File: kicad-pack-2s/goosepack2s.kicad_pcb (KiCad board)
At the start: 4 copper layers, 67 parts, among them J1 USB_C_Receptacle_USB2.0_16P, J11 Balance 2S, J2 Pack lead, J3 XT30UPB-M, Q2 IRF8736, Q3 IRF8736, Q4 AO3400A, Q5 AO3400A, U13 S-8252AAH, U21 HY2213-BB3A, U22 HY2213-BB3A, U7 BQ25798

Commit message: Fill in LCSC numbers, swap to stocked parts, tidy the new schematic parts
- LCSC numbers from JLC's 2026-10-19 in-stock catalog for every new part
  except the DRV8251A, which JLC doesn't stock (Global Sourcing or consign).
- 2S protector S-8252AAH -> HY2120-LB (C168778): pin-for-pin the same,
  OV 4.25 V / UV 2.80 V, stocked at JLC. R94 trip recovery still holds.
- IPROPI R101-R106 1.18k (2,341 in stock) -> 1.2k preferred (C25862),
  so the motor limit is 1.34 A.
- Fix the 2S pack board's footprint-symbol links (paths were dropped in
  the previous commit); both boards now link every footprint correctly.
- Move the VREF divider and the balancer block into clear space and
  rewrite the stale DRV8871/BQ7791501 notes on the motor and 2S sheets.

Co-Authored-By: Claude Opus 5.5 <noreply@anthropic.com>
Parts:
- U13: value S-8252AAH -> HY2120-LB
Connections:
- net /PROT_VM renamed /PROT_CS
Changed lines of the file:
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@@
 				(font
 					(size 1.27 1.27)
+					(thickness 0.15)
 				)
 			)
@@
 				(font
 					(size 1.27 1.27)
+					(thickness 0.15)
 				)
 			)
 		)
-		(property "LCSC Part #" ""
+		(property "LCSC Part #" "C144394"
 			(at 0 0 0)
 			(layer "F.Fab")
@@
 				(font
 					(size 1.27 1.27)
+					(thickness 0.15)
 				)
 			)
@@
 			)
 		)
-		(property "LCSC Part #" ""
+		(property "LCSC Part #" "C25762"
 			(at 0 0 0)
 			(layer "F.Fab")
@@
 				(font
 					(size 1.27 1.27)
+					(thickness 0.15)
 				)
 			)
@@
 				(font
 					(size 1.27 1.27)
+					(thickness 0.15)
 				)
 			)
@@
 				(font
 					(size 1.27 1.27)
+					(thickness 0.15)
 				)
 			)
@@
 				(font
 					(size 1.27 1.27)
+					(thickness 0.15)
 				)
 			)
@@
 				(font
 					(size 1.27 1.27)
+					(thickness 0.15)
 				)
 			)
@@
 				(font
 					(size 1.27 1.27)
+					(thickness 0.15)
 				)
 			)
@@
 				(font
 					(size 1.27 1.27)
+					(thickness 0.15)
 				)
 			)
@@
 				(font
 					(size 1.27 1.27)
+					(thickness 0.15)
 				)
 			)
@@
 				(font
 					(size 1.27 1.27)
+					(thickness 0.15)
 				)
 			)
@@
 				(font
 					(size 1.27 1.27)
+					(thickness 0.15)
 				)
 			)
@@
 				(font
 					(size 1.27 1.27)
+					(thickness 0.15)
 				)
 			)
@@
 				(font
 					(size 1.27 1.27)
+					(thickness 0.15)
 				)
 			)
@@
 				(font
 					(size 1.27 1.27)
+					(thickness 0.15)
 				)
 			)
@@
 				(font
 					(size 1.27 1.27)
+					(thickness 0.15)
 				)
 			)
@@
 				(font
 					(size 1.27 1.27)
+					(thickness 0.15)
 				)
 			)
@@
 			)
 		)
-		(property "LCSC Part #" ""
+		(property "LCSC Part #" "C25117"
 			(at 0 0 0)
 			(layer "F.Fab")
@@
 				(font
 					(size 1.27 1.27)
+					(thickness 0.15)
 				)
 			)
@@
 				(font
 					(size 1.27 1.27)
+					(thickness 0.15)
 				)
 			)
@@
 				(font
 					(size 1.27 1.27)
+					(thickness 0.15)
 				)
 			)
@@
 			)
 		)
-		(property "LCSC Part #" ""
+		(property "LCSC Part #" "C4109"
 			(at 0 0 0)
 			(layer "F.Fab")
@@
 			(layers "F.Cu" "F.Mask" "F.Paste")
 			(roundrect_rratio 0.25)
-			(net "/PROT_VM")
+			(net "/PROT_CS")
 		)
 		(pad "2" smd roundrect
@@
 			)
 		)
-		(property "LCSC Part #" ""
+		(property "LCSC Part #" "C17168"
 			(at 0 0 0)
 			(layer "F.Fab")
@@
 			)
 		)
-		(property "Value" "S-8252AAH"
+		(property "Value" "HY2120-LB"
 			(at 0 2.4 0)
 			(layer "F.Fab")
@@
 			)
 		)
-		(property "Datasheet" "https://www.ablic.com/en/doc/datasheet/battery_protection/S8252_E.pdf"
+		(property "Datasheet" "https://datasheet.lcsc.com/datasheet/pdf/90ce4cf43db74515b75ff3acebde0584.pdf"
 			(at 0 0 0)
 			(layer "F.Fab")
@@
 			)
 		)
-		(property "Description" "2-cell Li-ion protection IC, external low-side N-FETs, SOT-23-6"
+		(property "Description" "2-cell Li-ion protection IC, OV 4.25 V, UV 2.80 V, SOT-23-6"
 			(at 0 0 0)
 			(layer "F.Fab")
@@
 			)
 		)
-		(property "MPN" "S-8252AAH-M6T1U"
+		(property "MPN" "HY2120-LB"
 			(at 0 0 0)
 			(layer "F.Fab")
@@
 				(font
 					(size 1.27 1.27)
+					(thickness 0.15)
 				)
 			)
 		)
-		(property "Manufacturer" "ABLIC"
+		(property "Manufacturer" "HYCON"
 			(at 0 0 0)
 			(layer "F.Fab")
@@
 				(font
 					(size 1.27 1.27)
+					(thickness 0.15)
 				)
 			)
 		)
-		(property "LCSC Part #" ""
+		(property "LCSC Part #" "C168778"
 			(at 0 0 0)
 			(layer "F.Fab")
@@
 				(font
 					(size 1.27 1.27)
+					(thickness 0.15)
 				)
 			)
@@
 			(layers "F.Cu" "F.Mask" "F.Paste")
 			(roundrect_rratio 0.25)
-			(net "/PROT_VM")
+			(net "/PROT_CS")
 		)
 		(pad "4" smd roundrect
@@
 				(font
 					(size 1.27 1.27)
+					(thickness 0.15)
 				)
 			)
@@
 				(font
 					(size 1.27 1.27)
+					(thickness 0.15)
 				)
 			)
@@
 				(font
 					(size 1.27 1.27)
+					(thickness 0.15)
 				)
 			)
@@
 			)
 		)
-		(property "LCSC Part #" ""
+		(property "LCSC Part #" "C25117"
 			(at 0 0 0)
 			(layer "F.Fab")
@@
 				(font
 					(size 1.27 1.27)
+					(thickness 0.15)
 				)
 			)
@@
 				(font
 					(size 1.27 1.27)
+					(thickness 0.15)
 				)
 			)
@@
 				(font
 					(size 1.27 1.27)
+					(thickness 0.15)
 				)
 			)
@@
 				(font
 					(size 1.27 1.27)
+					(thickness 0.15)
 				)
 			)
@@
 				(font
 					(size 1.27 1.27)
+					(thickness 0.15)
 				)
 			)
@@
 				(font
 					(size 1.27 1.27)
+					(thickness 0.15)
 				)
 			)
@@
 				(font
 					(size 1.27 1.27)
+					(thickness 0.15)
 				)
 			)
@@
 				(font
 					(size 1.27 1.27)
+					(thickness 0.15)
 				)
 			)
 		)
-		(property "LCSC Part #" ""
+		(property "LCSC Part #" "C15261"
 			(at 0 0 0)
 			(layer "F.Fab")
@@
 				(font
 					(size 1.27 1.27)
+					(thickness 0.15)
 				)
 			)
@@
 				(font
 					(size 1.27 1.27)
+					(thickness 0.15)
 				)
 			)
@@
 				(font
 					(size 1.27 1.27)
+					(thickness 0.15)
 				)
 			)
@@
 				(font
 					(size 1.27 1.27)
+					(thickness 0.15)
 				)
 			)
@@
 			)
 		)
-		(property "LCSC Part #" ""
+		(property "LCSC Part #" "C25924"
 			(at 0 0 0)
 			(layer "F.Fab")
@@
 				(font
 					(size 1.27 1.27)
+					(thickness 0.15)
 				)
 			)
@@
 				(font
 					(size 1.27 1.27)
+					(thickness 0.15)
 				)
 			)
 		)
-		(property "LCSC Part #" ""
+		(property "LCSC Part #" "C15261"
 			(at 0 0 0)
 			(layer "F.Fab")
@@
 				(font
 					(size 1.27 1.27)
+					(thickness 0.15)
 				)
 			)
@@
 				(font
 					(size 1.27 1.27)
+					(thickness 0.15)
 				)
 			)
@@
 				(font
 					(size 1.27 1.27)
+					(thickness 0.15)
 				)
 			)
@@
 				(font
 					(size 1.27 1.27)
+					(thickness 0.15)
 				)
 			)

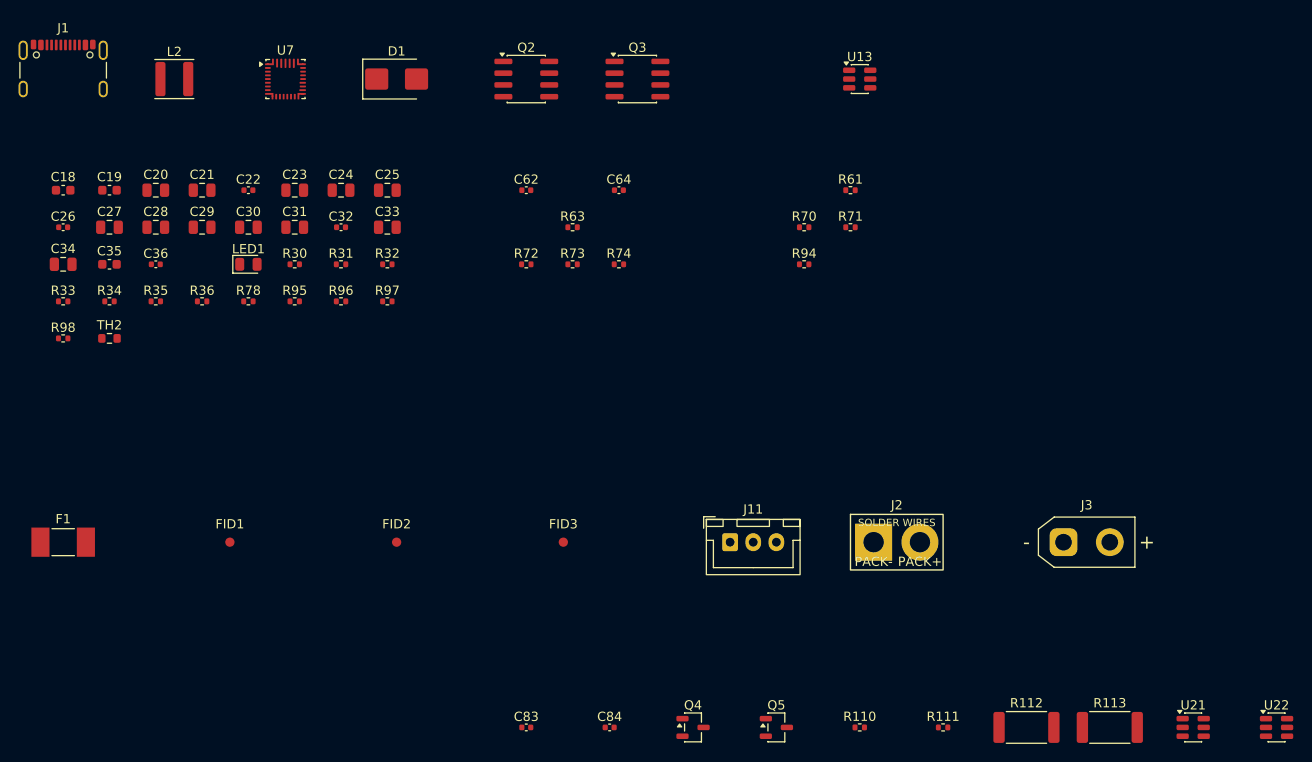
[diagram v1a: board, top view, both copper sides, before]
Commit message: Place and route the 2S pack board and add a --board switch to the pack tools
Every pack tool takes --board=pack2s (tools/packcfg.py); the 3S defaults and
placement are unchanged. The 2S board is 45 x 23 mm, routed with grid_router,
DRC-clean with schematic parity. The schematic is synced to the 3S fixes (J2/J3
pigtail pads, 0402 boot caps, SMBJ15A, RALEC R34), JLC places F1, L2, Q2 and Q3,
and TH2 became a fixed 10k R79 as on 3S. docs/2s-pack-process.md lists the
differences from the 3S process.

Co-Authored-By: Claude Opus 5.5 <noreply@anthropic.com>
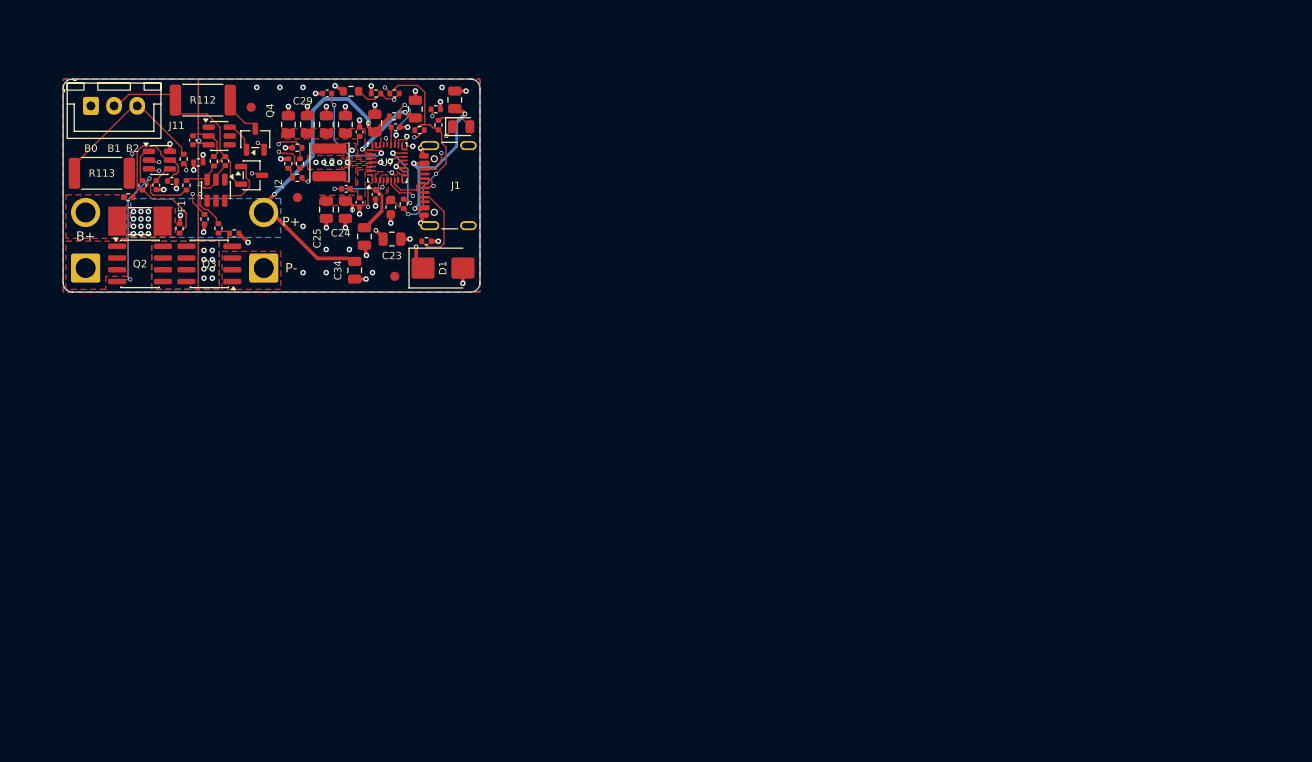
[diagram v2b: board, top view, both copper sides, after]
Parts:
- C18, C19: footprint Capacitor_SMD:C_0603_1608Metric -> Capacitor_SMD:C_0402_1005Metric
- D1: value SMBJ20A -> SMBJ15A
- J2: footprint hexy:XT30_SolderPads_1x02_P5.00mm -> Connector_Wire:SolderWire-1.5sqmm_1x02_P6mm_D1.7mm_OD3mm
- J3: value XT30UPB-M -> Cell pigtail; footprint hexy:AMASS_XT30UPB-M_1x02_P5.0mm_Vertical_EasyEDA3D -> Connector_Wire:SolderWire-1.5sqmm_1x02_P6mm_D1.7mm_OD3mm
- R79: renamed from TH2; value 10k B3434 -> 10k
- moved U22 128.4 mm to (116.5, 112.0), turned to -90 degrees
- moved R113 124.2 mm to (104.2, 110.2)
- moved U21 123.0 mm to (116.8, 106.1)
- moved R112 111.8 mm to (115.1, 102.3)
- moved J3 109.6 mm to (102.4, 120.4), turned to 90 degrees
- moved R111 102.4 mm to (113.0, 108.6), turned to -90 degrees
- moved R110 92.7 mm to (116.3, 108.9), turned to 90 degrees
- moved J11 83.5 mm to (103.0, 102.9)
- moved Q5 82.2 mm to (120.3, 110.4)
- moved Q4 79.2 mm to (120.7, 106.5), turned to 90 degrees
- moved R61 78.0 mm to (107.0, 112.8)
- moved U13 76.1 mm to (110.4, 108.7)
- moved J2 74.5 mm to (121.7, 120.4), turned to 90 degrees
- moved C84 73.9 mm to (117.5, 108.9), turned to 90 degrees
- moved C83 72.9 mm to (114.0, 106.6), turned to -90 degrees
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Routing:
- net /REGN: track 0.00 -> 40.4 mm, vias 0 -> 4
- net /PACK-: track 0.00 -> 32.2 mm, vias 0 -> 46
- net /PACK+: track 0.00 -> 30.5 mm, vias 0 -> 14
- net /VBUS: track 0.00 -> 27.7 mm, vias 0 -> 5
- net /ILIM_HIZ: track 0.00 -> 23.1 mm, vias 0 -> 2
- net /Q2_G: track 0.00 -> 21.1 mm, vias 0 -> 2
- net /CELL0: track 0.00 -> 19.7 mm, vias 0 -> 2
- net /CELL1: track 0.00 -> 19.5 mm
- net /STAT: track 0.00 -> 16.2 mm, vias 0 -> 2
- net /BAL2_D: track 0.00 -> 14.7 mm, vias 0 -> 2
- net /CELL2: track 0.00 -> 13.8 mm
- net /SDRV: track 0.00 -> 12.2 mm, vias 0 -> 2
- net /TS: track 0.00 -> 11.3 mm, vias 0 -> 2
- net /PROG: track 0.00 -> 11.3 mm, vias 0 -> 2
- net /PROT_VDD: track 0.00 -> 11.0 mm
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- added copper zone on B.Cu, net /BAT_N
- added copper zone on F.Cu, net /BAT_N
- added copper zone on In1.Cu, net /BAT_N
- added copper zone on In2.Cu, net /BAT_N
- added copper zone on F.Cu, net /CELL+
- added copper zone on F.Cu, net /CHG_SYS
- added copper zone on B.Cu, net /PACK+
- added copper zone on F.Cu, net /PACK+
- added copper zone on In2.Cu, net /PACK+
- added copper zone on B.Cu, net /PACK-
- added copper zone on F.Cu, net /PACK-
- added copper zone on In1.Cu, net /PACK-
- added copper zone on In2.Cu, net /PACK-
- added copper zone on F.Cu, net /PMID
- added copper zone on B.Cu, net /PROT_FET_D
- added copper zone on F.Cu, net /PROT_FET_D
- added copper zone on F.Cu, net /REGN
- added copper zone on F.Cu, net /SW1
- added copper zone on F.Cu, net /SW2
- added copper zone on F.Cu, net /VBUS
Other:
- board outline added: 45 x 23 mm
- board text added: "B+"
- board text added: "B-"
- board text added: "B0"
- board text added: "B1"
- board text added: "B2"
- board text added: "P+"
- board text added: "P-"
